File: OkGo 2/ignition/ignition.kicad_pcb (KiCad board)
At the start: 2 copper layers, 96 parts, among them K201 16A SPST, K202 16A SPST, K203 16A SPST, K204 16A SPST, K205 16A SPST, P105 BATT, P106 SMA, P107 ARM_LED, P201 CH3_LED, P203 CH3, P204 CH1_LED, P206 CH1, P207 CH4_LED, P209 CH4, P210 CH2_LED, P212 CH2, Q201 BSS138BK, Q202 BSS138BK, Q203 BSS138BK, Q204 BSS138BK, Q205 BSS138BK, U103 SWD, U105 RFM95W, U106 STM32F071CBT6, U107 TSR 0.5-2433, Y101 8MHz

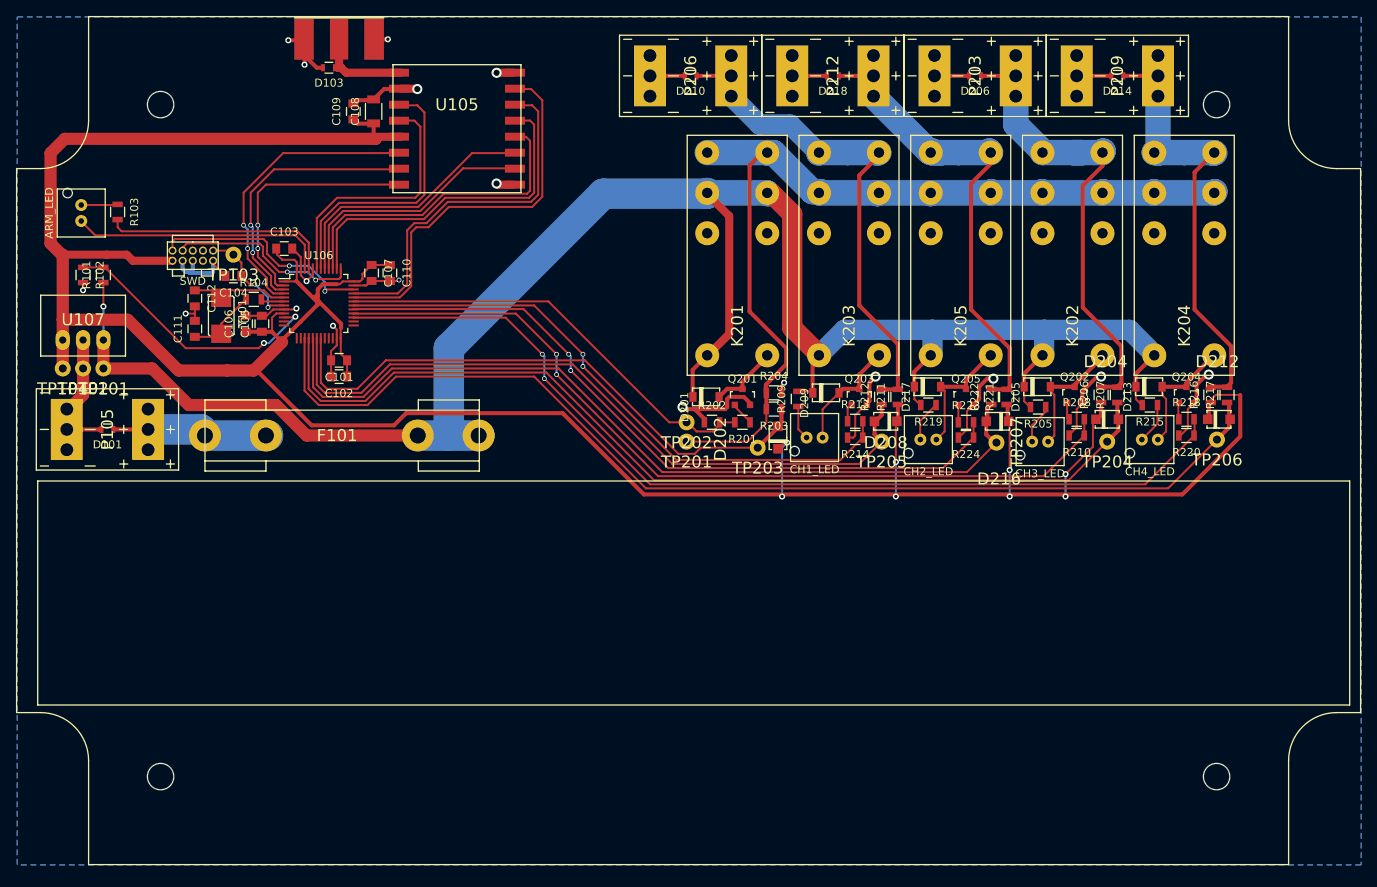
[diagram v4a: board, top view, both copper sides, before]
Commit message: Fixed #28, fixed #24, general tidying
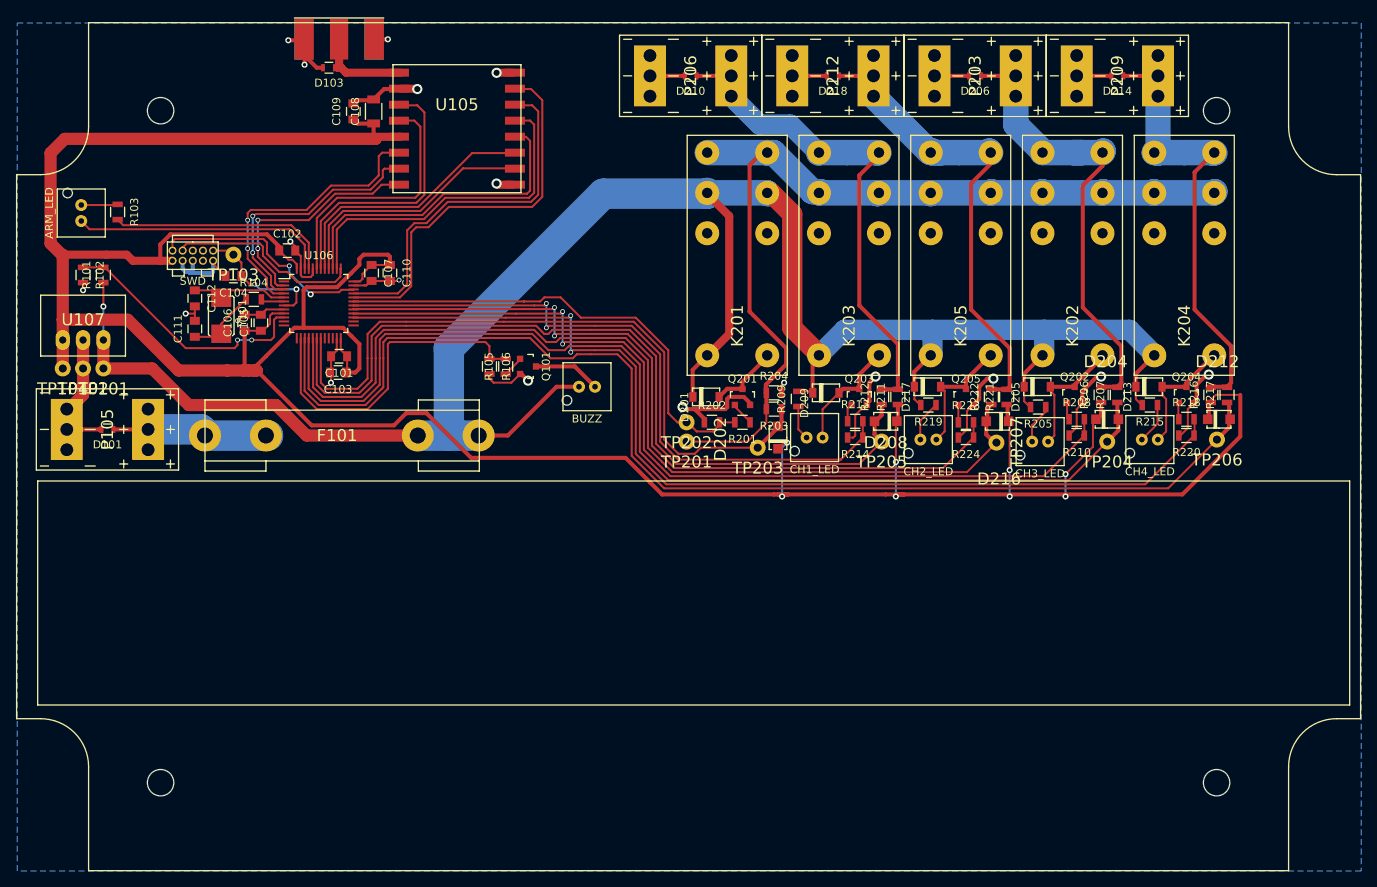
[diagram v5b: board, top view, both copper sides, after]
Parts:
- added P109: BUZZ, ignition:JST-PA-2-VERT, F.Cu at (109.2, 94.2)
- added Q101: BSS138BK, Housings_SOT-23_SOT-143_TSOT-6:SOT-23, F.Cu at (101.9, 91.7)
- added R105: 180R, Resistors_SMD:R_0805, F.Cu at (99.1, 91.7)
- added R106: 100k, Resistors_SMD:R_0805, F.Cu at (97.0, 91.7)
- moved C102 17.0 mm to (71.8, 77.2), turned to 0 degrees
- moved C103 16.9 mm to (78.1, 92.5), turned to 180 degrees
- moved REF** 0.76 mm to (121.9, 101.7)
- moved C101 0.51 mm to (78.2, 90.4)
- moved C105 0.18 mm to (68.5, 86.2)
- moved C106 0.18 mm to (66.4, 86.2)
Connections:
- U103 pad 6: (no net) -> Net-(U103-Pad6)
- U103 pad 7: (no net) -> Net-(U103-Pad7)
- U103 pad 8: (no net) -> Net-(U103-Pad8)
- U106 pad 11: (no net) -> Net-(U106-Pad11)
- U106 pad 12: (no net) -> Net-(U106-Pad12)
- U106 pad 13: (no net) -> Net-(U106-Pad13)
- U106 pad 14: (no net) -> /BUZZER
- U106 pad 20: (no net) -> Net-(U106-Pad20)
- U106 pad 21: (no net) -> Net-(U106-Pad21)
- U106 pad 22: (no net) -> Net-(U106-Pad22)
- U106 pad 25: (no net) -> Net-(U106-Pad25)
- U106 pad 26: (no net) -> Net-(U106-Pad26)
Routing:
- net /BUZZER: track 0.00 -> 41.9 mm
- net +3V3: track 368.1 -> 401.4 mm
- net +BATT: track 255.6 -> 270.7 mm
- net /firing/CONT_CH4: track 136.8 -> 151.0 mm
- net /firing/CONT_CH3: track 121.5 -> 135.6 mm
- net /firing/CONT_CH1: track 90.9 -> 105.0 mm
- net /firing/CONT_CH2: track 106.6 -> 120.7 mm
- net /firing/RELAY_SENSE: track 73.2 -> 86.9 mm
- net Net-(P109-Pad1): track 0.00 -> 8.42 mm
- net /firing/FIRE_CH4: track 120.0 -> 127.9 mm
- net /firing/FIRE_CH2: track 90.4 -> 98.2 mm
- net /firing/FIRE_CH1: track 75.9 -> 83.6 mm
- net /firing/FIRE_CH3: track 105.7 -> 113.4 mm
- net GND: track 150.9 -> 156.5 mm, vias 18 -> 19
- net /firing/UPSTREAM_RELAY: track 55.3 -> 60.4 mm
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
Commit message: Fixes #22
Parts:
- removed the REF** at (121.9, 101.7)
- added M3_MOUNT: VAL**, common:M3_MOUNT_FANCY, F.Cu at (55.9, 143.7)
- added M3_MOUNT: VAL**, common:M3_MOUNT_FANCY, F.Cu at (187.9, 143.7)
- added M3_MOUNT: VAL**, common:M3_MOUNT_FANCY, F.Cu at (187.9, 59.7)
- added M3_MOUNT: VAL**, common:M3_MOUNT_FANCY, F.Cu at (55.9, 59.7)
- moved R103 2.68 mm to (53.2, 72.6), turned to 0 degrees
- moved C109 2.54 mm to (82.5, 59.9)
- moved P107 2.48 mm to (48.1, 73.8)
- moved C108 2.42 mm to (80.1, 59.9)
- moved D103 2.22 mm to (75.1, 55.5)
- moved P106 1.66 mm to (76.8, 51.7)
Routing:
- net +3V3: track 401.4 -> 392.0 mm
- net /ARM_LED: track 28.4 -> 25.1 mm
- net GND: track 156.5 -> 153.8 mm, vias 19 -> 18
- net /DISARM_LED: track 32.2 -> 29.7 mm
- net Net-(P107-Pad2): track 4.82 -> 4.20 mm
- net Net-(D103-Pad1): track 13.9 -> 14.4 mm
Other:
- board outline added: 167.9 x 105.9 mm

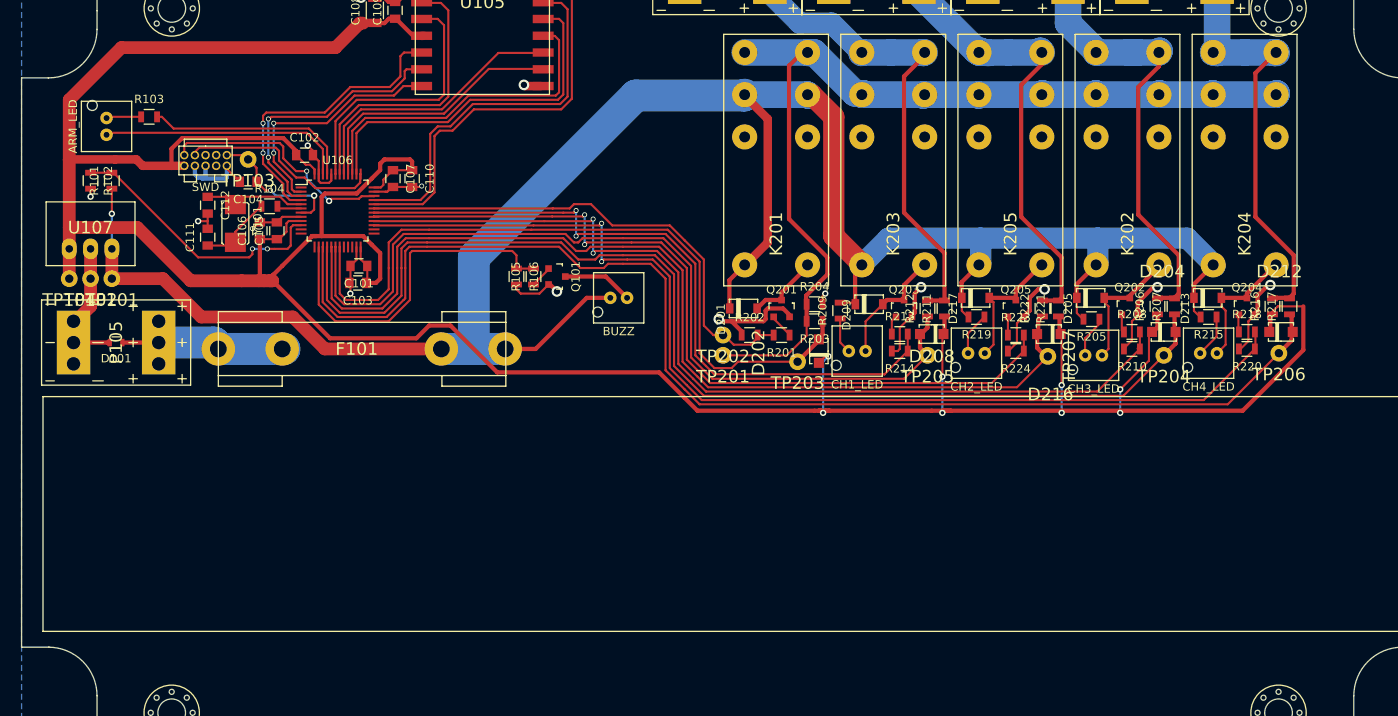
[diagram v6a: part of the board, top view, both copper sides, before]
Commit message: LiPo cable tie holes, resolves #26
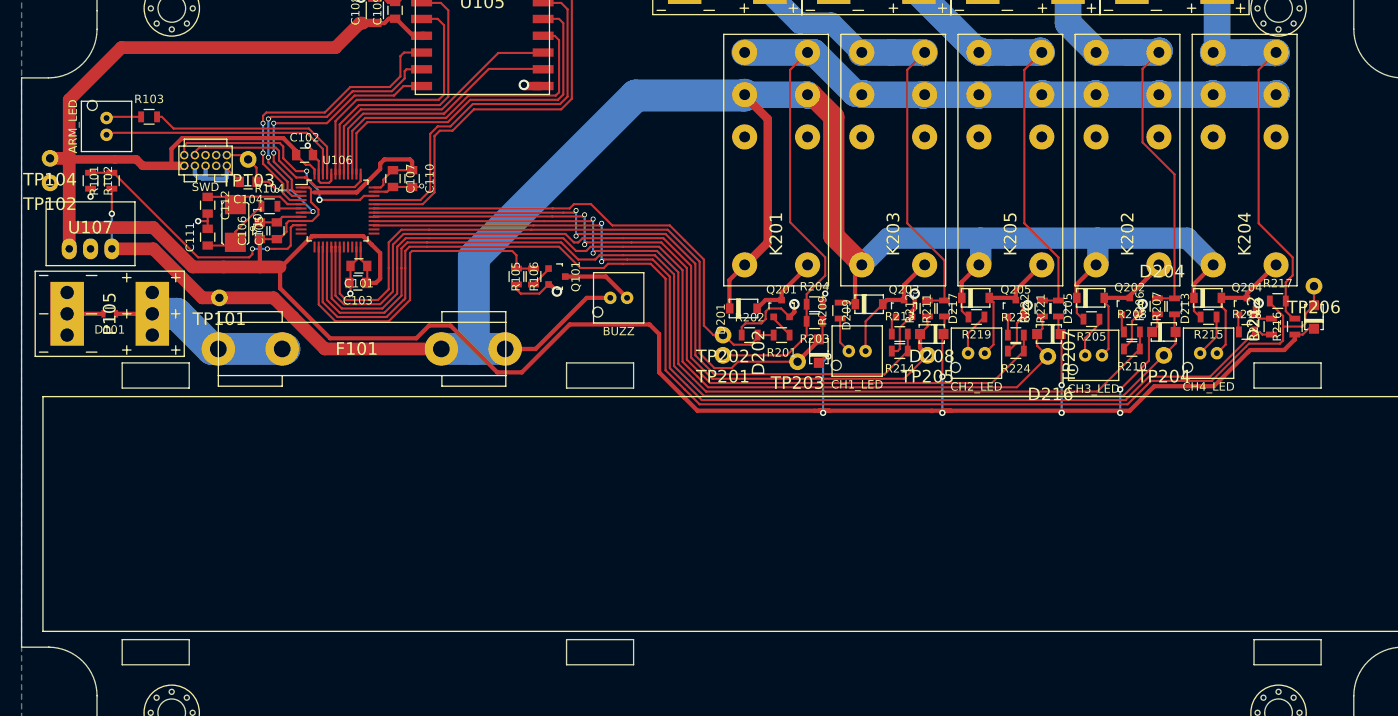
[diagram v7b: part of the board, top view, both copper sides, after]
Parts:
- moved TP104 14.5 mm to (41.4, 77.6)
- moved TP101 13.0 mm to (61.6, 94.2)
- moved TP102 12.4 mm to (41.4, 80.5)
- moved TP206 9.03 mm to (192.2, 92.8)
- moved D212 4.32 mm to (192.2, 96.5), turned to 270 degrees
- moved R220 3.96 mm to (187.1, 97.7), turned to 90 degrees
- moved R216 3.60 mm to (189.9, 97.7)
- moved D101 3.51 mm to (48.5, 96.1)
- moved P105 3.51 mm to (48.5, 96.1)
- moved R217 1.53 mm to (187.8, 94.6), turned to 0 degrees
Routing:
- net GND: track 153.8 -> 128.5 mm
- net /firing/CONT_CH4: track 151.0 -> 159.5 mm
- net +3V3: track 392.0 -> 386.9 mm
- net +BATT: track 270.7 -> 268.4 mm
- net Net-(D101-Pad1): track 25.9 -> 27.4 mm
- net /nRST: track 16.8 -> 15.5 mm
- net /firing/FIRE_CH4: track 127.9 -> 128.7 mm
- net Net-(D206-Pad1): track 63.3 -> 62.6 mm
- net /firing/CONT_CH1: track 105.0 -> 104.3 mm
- net /firing/CONT_CH2: track 120.7 -> 120.1 mm
- net Net-(D218-Pad1): track 64.5 -> 63.9 mm
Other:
- outline, holes or cut-outs redrawn

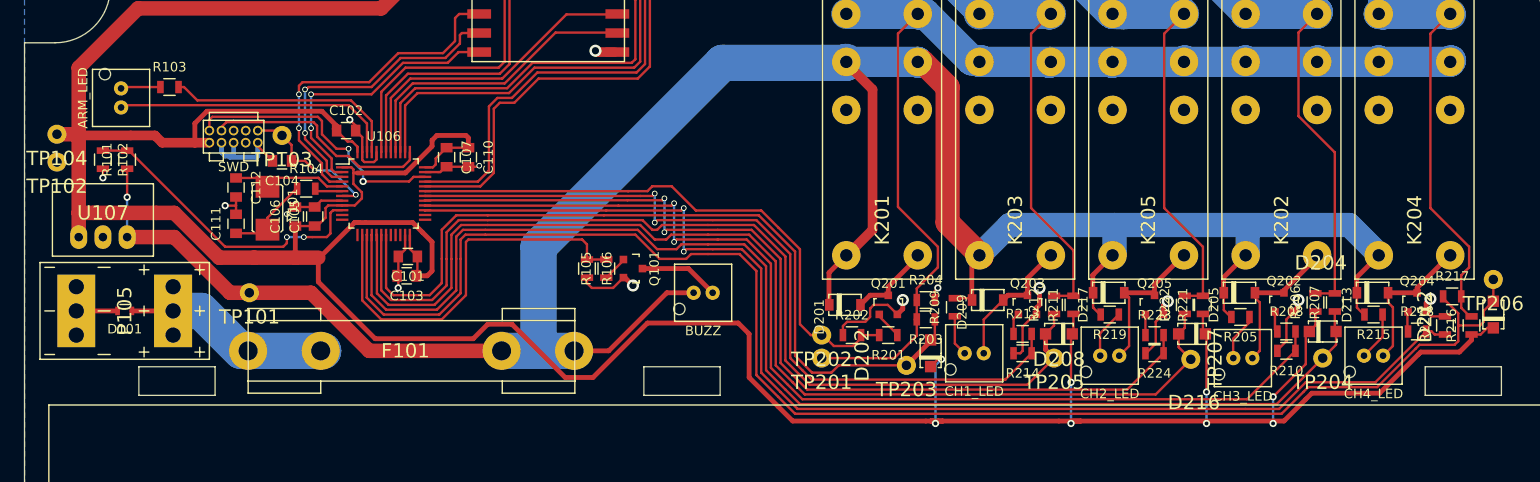
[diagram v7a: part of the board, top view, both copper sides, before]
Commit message: Corrected a bunch of footprints, see #9
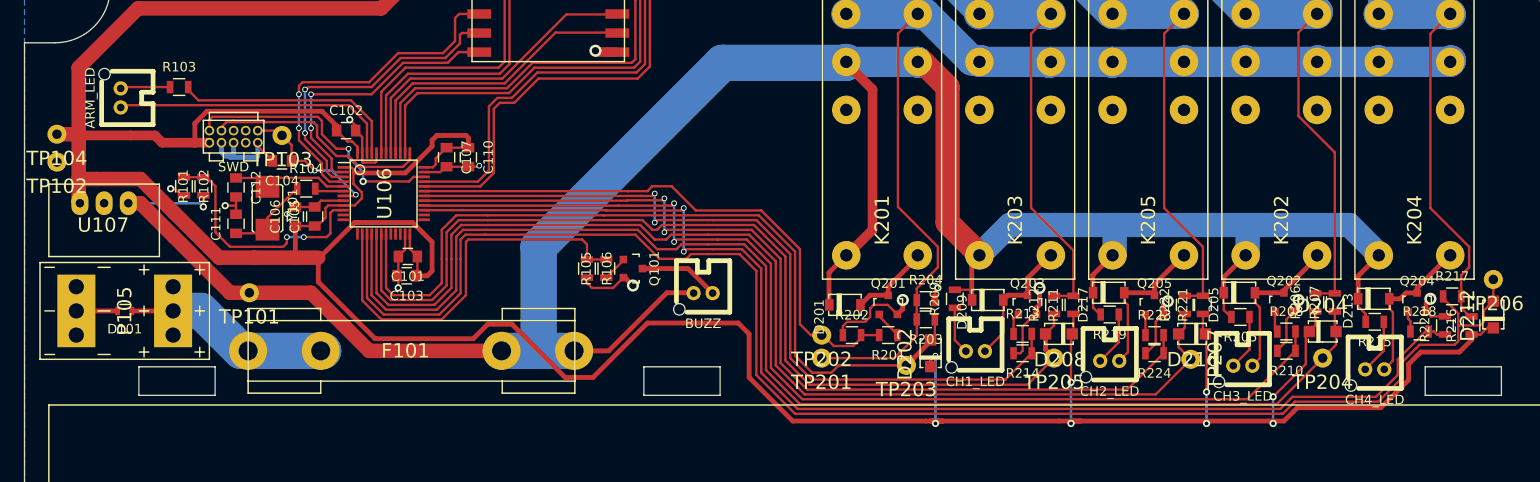
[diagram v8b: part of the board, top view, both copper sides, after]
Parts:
- U106: footprint Housings_QFP:LQFP-48_7x7mm_Pitch0.5mm -> common:LQFP48_ST
- moved R102 8.96 mm to (54.7, 83.1)
- moved R101 8.47 mm to (56.8, 83.1)
- moved U107 3.56 mm to (46.4, 84.8)
- moved P204 1.02 mm to (137.8, 99.6)
- moved R103 1.02 mm to (54.2, 72.6)
- moved R209 0.89 mm to (135.6, 94.9)
- moved R215 0.77 mm to (179.7, 97.3)
- moved P107 0.76 mm to (48.9, 73.8)
- moved P109 0.76 mm to (109.2, 93.5)
- moved D213 0.65 mm to (179.7, 94.9)
- moved P207 0.65 mm to (179.7, 101.5)
- moved P210 0.25 mm to (151.9, 100.6)
- moved R218 0.25 mm to (184.4, 98.3)
- turned U106 to 270 degrees
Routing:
- net /BATT_MON: track 32.9 -> 25.7 mm
- net +BATT: track 268.4 -> 272.4 mm
- net Net-(P107-Pad2): track 4.20 -> 5.24 mm
- net /firing/FIRE_CH4: track 128.7 -> 129.7 mm
- net /firing/CONT_CH4: track 159.5 -> 160.5 mm
- net /ARM_LED: track 25.1 -> 24.2 mm
- net Net-(D213-Pad2): track 16.0 -> 16.9 mm
- net GND: track 128.5 -> 129.3 mm
- net Net-(D205-Pad2): track 15.9 -> 16.7 mm
- net Net-(P207-Pad2): track 5.15 -> 5.80 mm
- net Net-(P210-Pad2): track 5.15 -> 5.69 mm
